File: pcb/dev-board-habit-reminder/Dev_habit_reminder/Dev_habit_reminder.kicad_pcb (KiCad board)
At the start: 2 copper layers, 83.8 x 71.1 mm, 13 parts, among them J1 I2C BREAKOUT, SW1 SW_Push, SW2 SW_Push, SW3 SW_Push, U1 ESP32-DevKitC

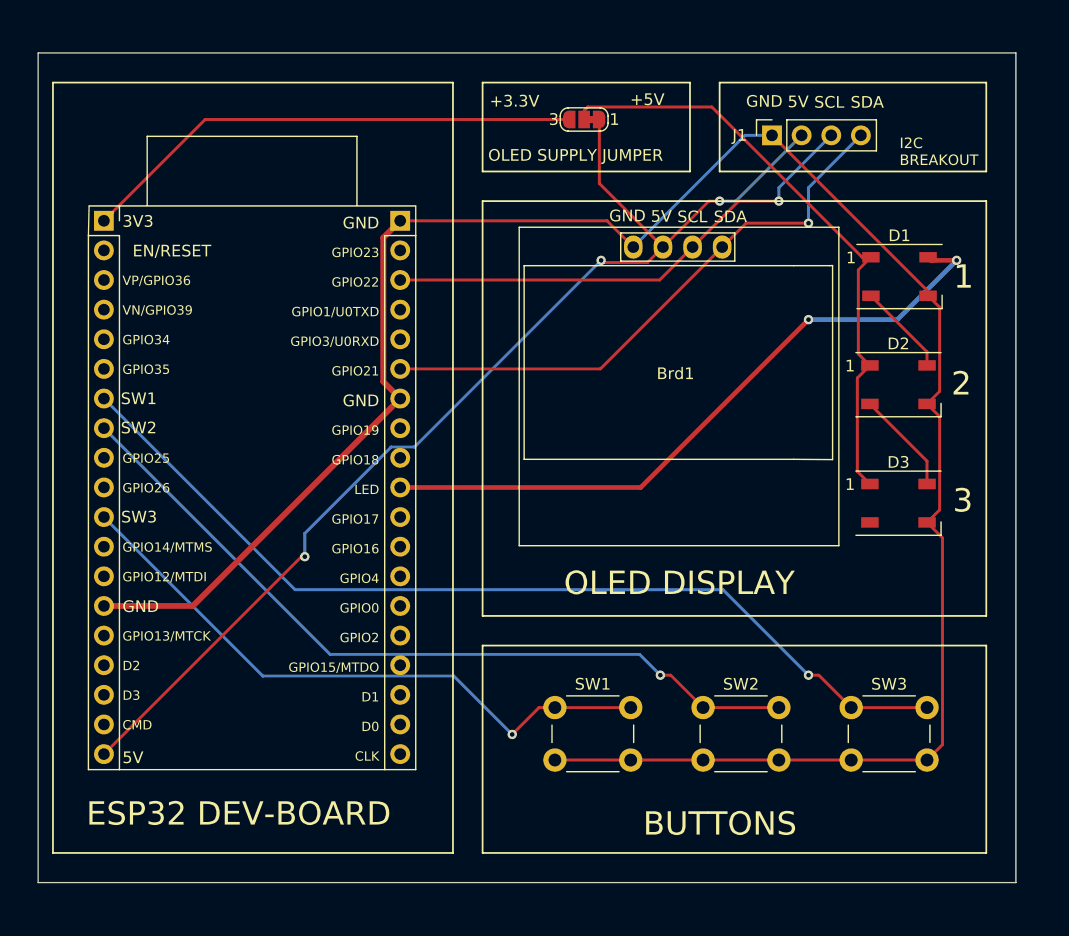
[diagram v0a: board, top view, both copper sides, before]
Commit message: PCB Track width definition, rerouting
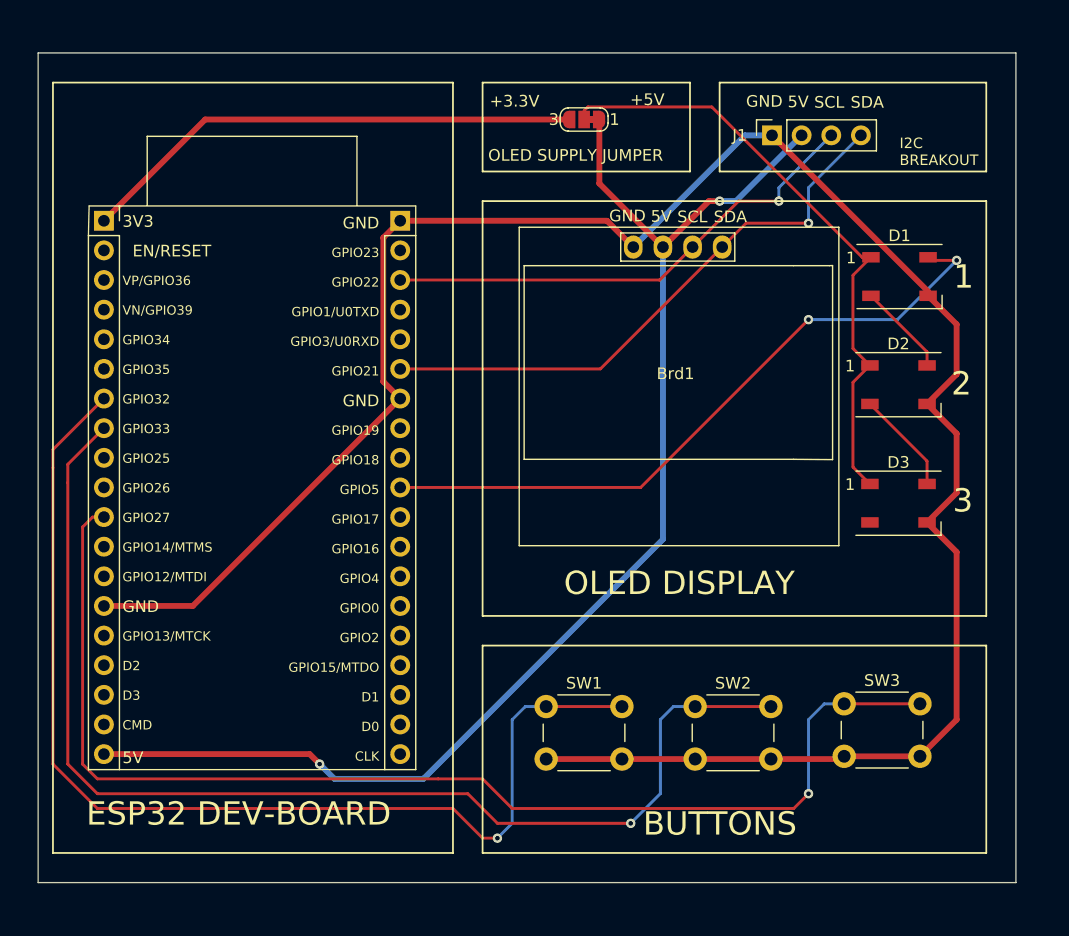
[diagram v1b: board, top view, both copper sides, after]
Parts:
- moved SW1 26.2 mm to (150.2, 114.4)
- moved REF** 26.2 mm to (165.1, 99.1)
- moved SW3 24.8 mm to (175.8, 114.2)
- moved REF** 15.2 mm to (144.8, 121.9)
- moved REF** 8.03 mm to (121.9, 119.4)
- moved SW2 0.68 mm to (163.0, 114.4)
- renumbered SW3 to SW1, SW1 to SW3
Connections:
- net Net-(D1-VDD) renamed /OLED_PWR
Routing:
- net /SW3: track 53.8 -> 103.3 mm
- net /SW2: track 67.8 -> 100.3 mm
- net +5V: track 96.3 -> 111.4 mm, vias 3 -> 2
- net /SW1: track 81.5 -> 94.4 mm
- net GND: track 179.8 -> 183.4 mm
- net /OLED_PWR: track 52.0 -> 52.7 mm
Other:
- board text removed: "SW1"
- board text removed: "SW2"
- board text removed: "SW3"

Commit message: Added ground area and production files
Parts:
- moved REF** 46.0 mm to (124.5, 77.5)
- moved REF** 31.5 mm to (124.5, 97.8)
- moved REF** 3.59 mm to (124.5, 116.8)
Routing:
- added copper zone on B.Cu, net GND
- added copper zone on F.Cu, net GND
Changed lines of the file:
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@@
       (outputformat 1)
       (mirror false)
-      (drillshape 1)
+      (drillshape 0)
       (scaleselection 1)
-      (outputdirectory "")
+      (outputdirectory "./Gerber/")
     )
   )
@@
   )
   (footprint "Symbol:ESD-Logo_13.2x12mm_SilkScreen" (layer "B.Cu")
-    (at 121.92 119.38 180)
+    (at 124.46 116.84 180)
     (descr "Electrostatic discharge Logo")
     (tags "Logo ESD")
@@
   )
   (footprint "Symbol:OSHW-Logo_11.4x12mm_SilkScreen" (layer "B.Cu")
-    (at 144.78 121.92 180)
+    (at 124.46 97.79 180)
     (descr "Open Source Hardware Logo")
     (tags "Logo OSHW")
@@
   )
   (footprint "Symbol:KiCad-Logo2_6mm_SilkScreen" (layer "B.Cu")
-    (at 165.1 99.06 180)
+    (at 124.46 77.47 180)
     (descr "KiCad Logo")
     (tags "Logo KiCad")
@@
   (segment (start 147.32 124.46) (end 147.32 115.57) (width 0.25) (layer "B.Cu") (net 13))
   (segment (start 146.05 125.73) (end 147.32 124.46) (width 0.25) (layer "B.Cu") (net 13))
+  (zone (net 2) (net_name "GND") (layers "F&B.Cu") (hatch edge 0.5)
+    (connect_pads (clearance 0.5))
+    (min_thickness 0.25) (filled_areas_thickness no)
+    (fill yes (thermal_gap 0.5) (thermal_bridge_width 0.5))
+    (polygon
+      (pts
+        (xy 105.41 57.15)
+        (xy 105.41 132.08)
+        (xy 193.04 132.08)
+        (xy 193.04 57.15)
+      )
+    )
+  )
 )

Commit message: Board re-routing
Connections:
- net /OLED_PWR renamed /NEOPIXEL_PWR
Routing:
- net /SW2: track 100.3 -> 6.50 mm, vias 1 -> 0
- net /SW1: track 94.4 -> 6.50 mm, vias 1 -> 0
- net /LED: track 58.3 -> 0.00 mm, vias 2 -> 0
- net /SDA: track 49.6 -> 0.00 mm, vias 1 -> 0
- net /SCL: track 42.8 -> 0.00 mm, vias 1 -> 0
- net +5V: track 111.4 -> 124.7 mm, vias 2 -> 1
- net GND: track 183.4 -> 171.8 mm, vias 0 -> 2
- net +3.3V: track 43.5 -> 49.0 mm
- net /SW3: track 103.3 -> 108.7 mm
- net /NEOPIXEL_PWR: track 52.7 -> 53.9 mm
- removed copper zone on B.Cu, net GND
- removed copper zone on F.Cu, net GND
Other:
- board text added: "LED SUPPLY JUMPER"
- board text removed: "OLED SUPPLY JUMPER"

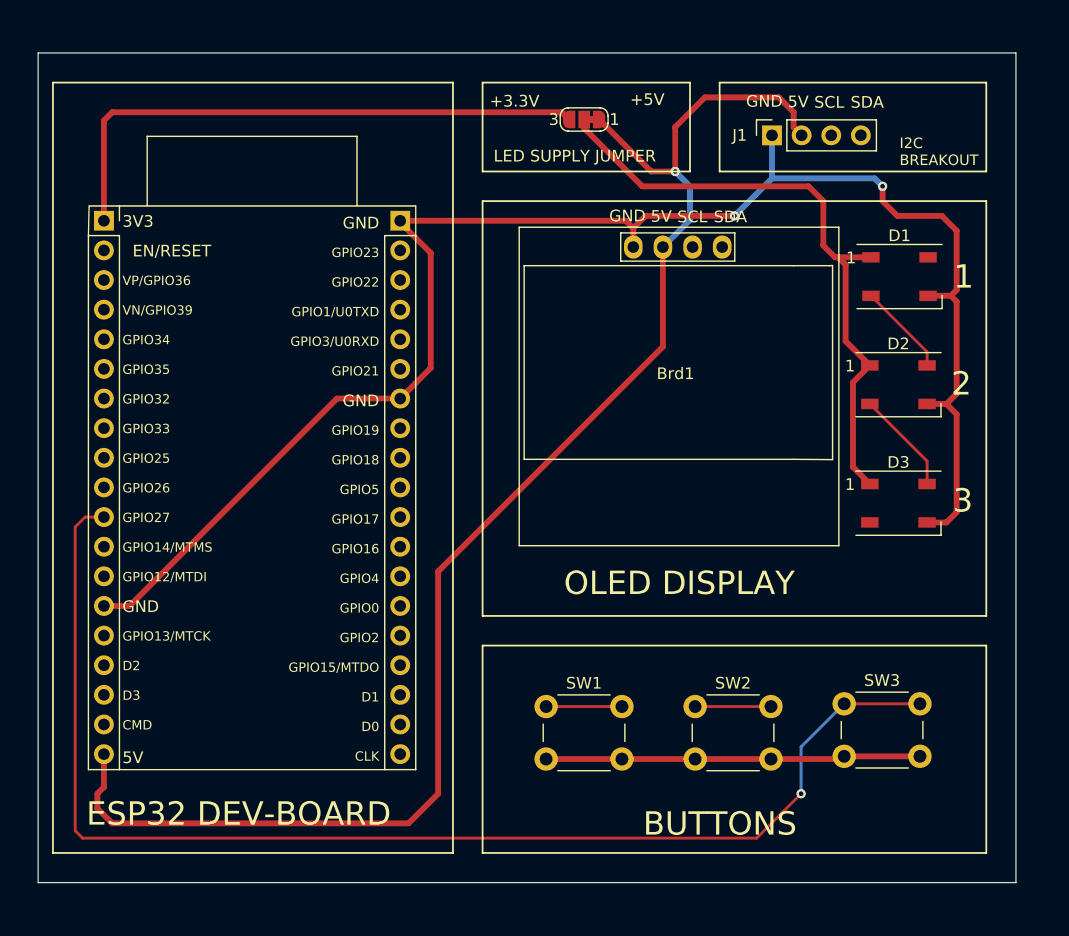
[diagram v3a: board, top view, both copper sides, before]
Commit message: Changed button pins for efficient routing
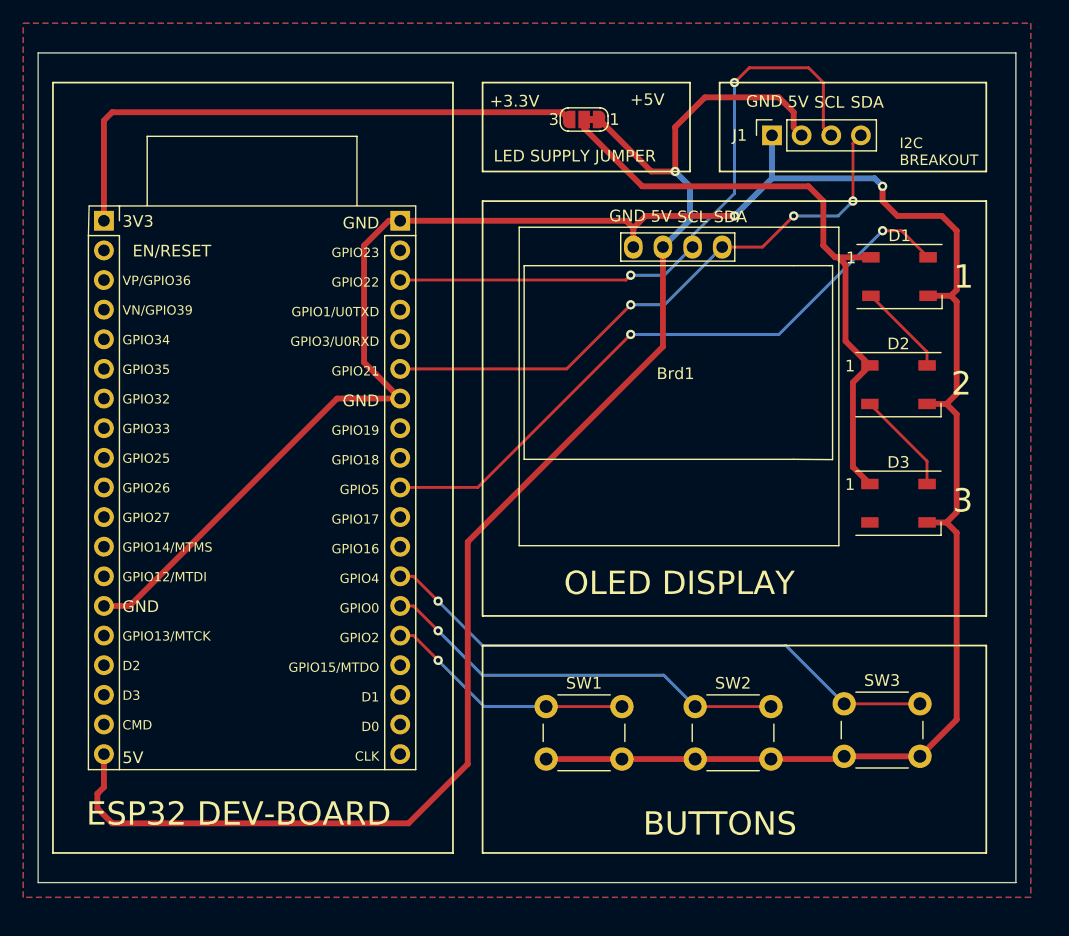
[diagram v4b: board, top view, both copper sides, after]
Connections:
- U1 pad 11: /SW3 -> unconnected-(U1-ADC2_CH7/GPIO27-Pad11)
- U1 pad 24: unconnected-(U1-ADC2_CH2/GPIO2-Pad24) -> /SW1
- U1 pad 25: unconnected-(U1-GPIO0/BOOT/ADC2_CH1-Pad25) -> /SW2
- U1 pad 26: unconnected-(U1-ADC2_CH0/GPIO4-Pad26) -> /SW3
- U1 pad 7: /SW1 -> unconnected-(U1-32K_XP/GPIO32/ADC1_CH4-Pad7)
- U1 pad 8: /SW2 -> unconnected-(U1-32K_XN/GPIO33/ADC1_CH5-Pad8)
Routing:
- net /SW3: track 108.7 -> 49.1 mm
- net /LED: track 0.00 -> 55.3 mm, vias 0 -> 2
- net /SCL: track 0.00 -> 55.3 mm, vias 0 -> 2
- net /SDA: track 0.00 -> 50.7 mm, vias 0 -> 3
- net /SW2: track 6.50 -> 35.4 mm, vias 0 -> 1
- net GND: track 171.8 -> 194.6 mm
- net /SW1: track 6.50 -> 21.5 mm, vias 0 -> 1
- added copper zone on B.Cu, net GND
- added copper zone on F.Cu, net GND
